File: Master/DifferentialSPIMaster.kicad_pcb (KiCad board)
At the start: 2 copper layers, 52.7 x 36.2 mm, 39 parts, among them J1 Motor Encoder 0, J2 Conn_01x20, J3 Motor Encoder 0, U1 SN65HVD06D, U2 SN65HVD06D, U3 SN65HVD06D, U4 SN65HVD06D, U5 SN65HVD06D, U6 SN65HVD06D

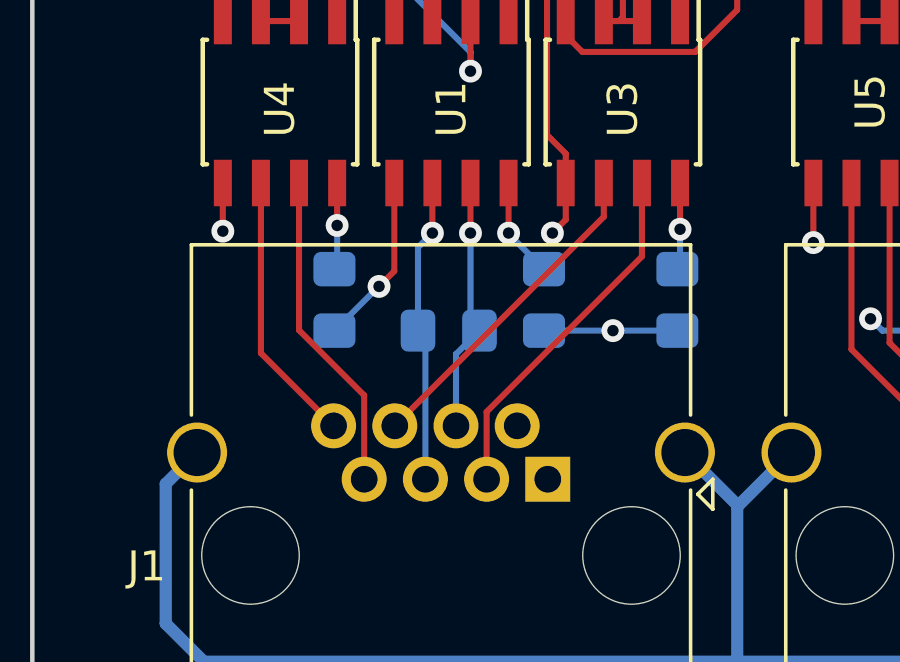
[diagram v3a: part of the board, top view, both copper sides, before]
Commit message: differential tuning on master
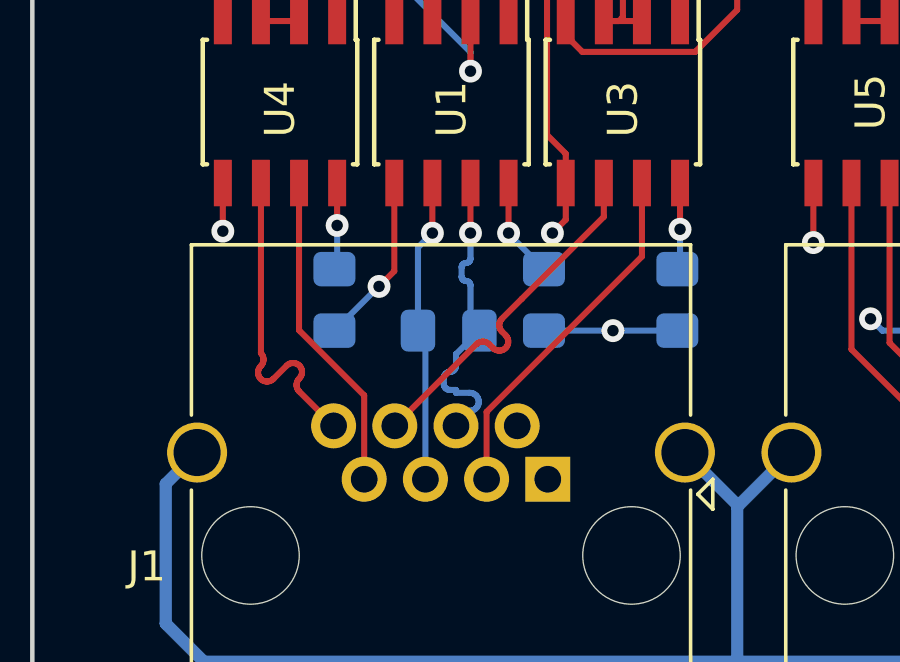
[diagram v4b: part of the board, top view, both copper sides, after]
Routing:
- net /MISO_1_-: track 8.54 -> 10.6 mm
- net /CS_1_+: track 9.10 -> 10.8 mm
- net /CLK_1_+: track 11.0 -> 12.0 mm

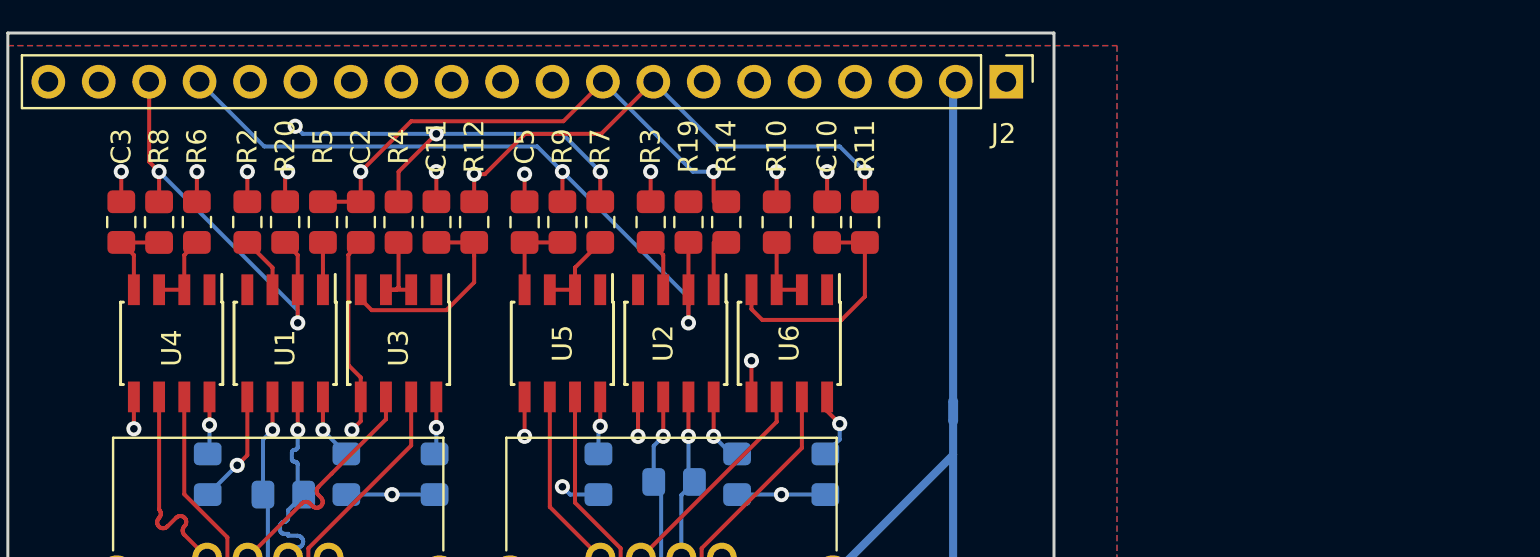
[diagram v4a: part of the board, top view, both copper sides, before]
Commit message: Swap to MAX14783 on Master
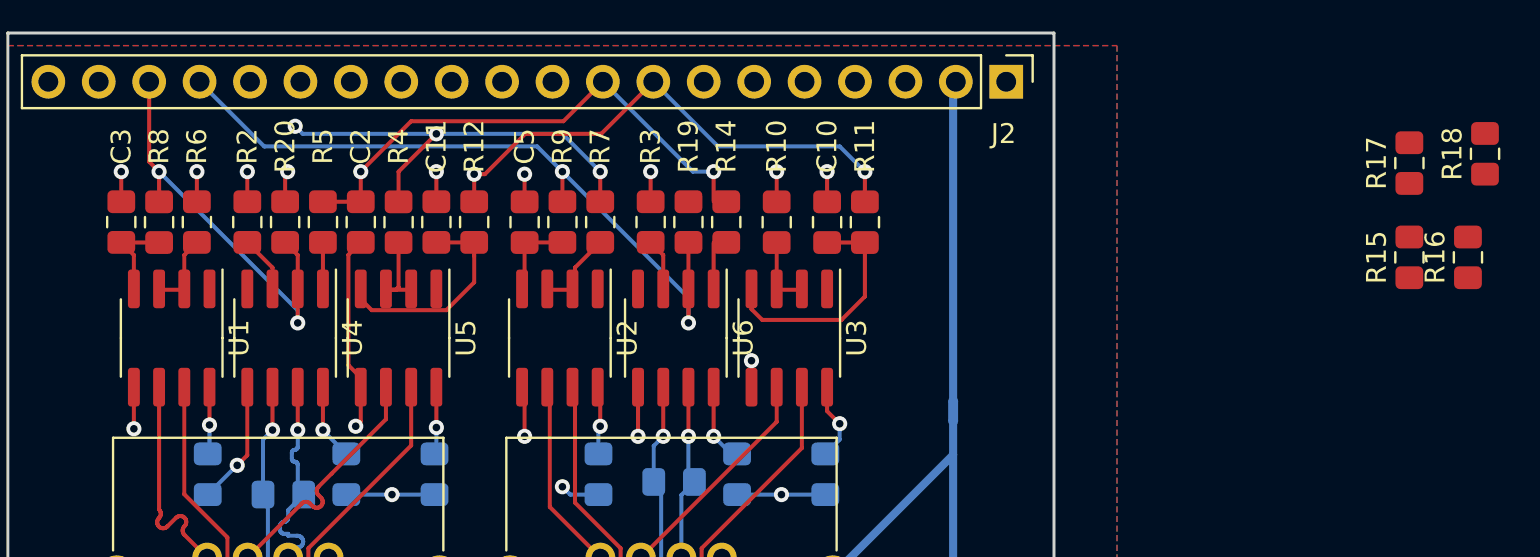
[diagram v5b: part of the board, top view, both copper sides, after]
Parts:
- added R15: 120, Resistor_SMD:R_0805_2012Metric_Pad1.15x1.40mm_HandSolder, F.Cu at (164.5, 98.4)
- added R16: 120, Resistor_SMD:R_0805_2012Metric_Pad1.15x1.40mm_HandSolder, F.Cu at (167.4, 98.4)
- added R17: 120, Resistor_SMD:R_0805_2012Metric_Pad1.15x1.40mm_HandSolder, F.Cu at (164.5, 93.6)
- added R18: 120, Resistor_SMD:R_0805_2012Metric_Pad1.15x1.40mm_HandSolder, F.Cu at (168.3, 93.2)
- U1, U2, U3, U4, U5, U6: value SN65HVD06D -> MAX14783ExS
- moved U3 19.7 mm to (133.2, 102.4)
- moved U5 8.26 mm to (113.5, 102.4)
- moved U2 5.85 mm to (121.7, 102.4)
- moved U1 5.72 mm to (102.1, 102.4)
- moved U4 5.72 mm to (107.8, 102.4)
- moved U6 5.72 mm to (127.5, 102.4)
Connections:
- U1 pad 1: Net-(R5-Pad2) -> Net-(U1-Pad1)
- U1 pad 2: /CS_1 -> Net-(R6-Pad2)
- U1 pad 3: Net-(R2-Pad1) -> Net-(R6-Pad2)
- U1 pad 4: Net-(U1-Pad4) -> Net-(C3-Pad1)
- U1 pad 6: /MISO_1_+ -> /CS_1_+
- U1 pad 7: /MISO_1_- -> /CS_1_-
- U2 pad 1: Net-(R14-Pad2) -> Net-(U2-Pad1)
- U2 pad 2: /CS_2 -> Net-(R7-Pad2)
- U2 pad 3: Net-(R3-Pad1) -> Net-(R7-Pad2)
- U2 pad 4: Net-(U2-Pad4) -> Net-(C5-Pad1)
- U2 pad 6: /MISO_2_+ -> /CS_2_+
- U2 pad 7: /MISO_2_- -> /CS_2_-
- U3 pad 2: Net-(R4-Pad2) -> Net-(R10-Pad2)
- U3 pad 3: Net-(R4-Pad2) -> Net-(R10-Pad2)
- U3 pad 4: Net-(C11-Pad1) -> Net-(C10-Pad1)
- U3 pad 6: /CLK_1_+ -> /CLK_2_+
- U3 pad 7: /CLK_1_- -> /CLK_2_-
- U4 pad 1: Net-(U4-Pad1) -> Net-(R5-Pad2)
- U4 pad 2: Net-(R6-Pad2) -> /CS_1
- U4 pad 3: Net-(R6-Pad2) -> Net-(R2-Pad1)
- U4 pad 4: Net-(C3-Pad1) -> Net-(U4-Pad4)
- U4 pad 6: /CS_1_+ -> /MISO_1_+
- U4 pad 7: /CS_1_- -> /MISO_1_-
- U5 pad 2: Net-(R7-Pad2) -> Net-(R4-Pad2)
- U5 pad 3: Net-(R7-Pad2) -> Net-(R4-Pad2)
- U5 pad 4: Net-(C5-Pad1) -> Net-(C11-Pad1)
- U5 pad 6: /CS_2_+ -> /CLK_1_+
- U5 pad 7: /CS_2_- -> /CLK_1_-
- U6 pad 1: Net-(U6-Pad1) -> Net-(R14-Pad2)
- U6 pad 2: Net-(R10-Pad2) -> /CS_2
- U6 pad 3: Net-(R10-Pad2) -> Net-(R3-Pad1)
- U6 pad 4: Net-(C10-Pad1) -> Net-(U6-Pad4)
- U6 pad 6: /CLK_2_+ -> /MISO_2_+
- U6 pad 7: /CLK_2_- -> /MISO_2_-

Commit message: Update master
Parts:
- removed H1, H2: MountingHole, MountingHole:MountingHole_3.5mm
- C1: value 100nF -> C_Small; moved to F.Cu
- C10, C11, C3: value 2.2pF -> C_Small
- C4, C6, C7, C8, C9, R1: moved to F.Cu
- C5: value 2.2pF -> 100nF
- J1: value Motor Encoder 0 -> RJ45_Shielded
- J2: value Conn_01x20 -> RJ45_Shielded; footprint Connector_PinHeader_2.54mm:PinHeader_1x20_P2.54mm_Vertical -> Connector_RJ:RJ45_Amphenol_RJHSE5380
- J3: value Motor Encoder 0 -> Conn_01x20; footprint Connector_RJ:RJ45_Amphenol_RJHSE5380 -> Connector_PinSocket_2.54mm:PinSocket_1x20_P2.54mm_Vertical
- NT1: value Net-Tie_2 -> NetTie_2; moved to F.Cu
- R10, R2, R7, R8, R9: value 1k -> 120
- R11, R12, R14, R3, R4: value 1k -> R_Small
- R13: value 120 -> 1k; moved to F.Cu
- R15, R17, R18: value 120 -> 1k
- R16: value 120 -> R_Small
- R19, R20: value 10k -> 1k
- moved R16 74.1 mm to (94.9, 83.3), turned to 0 degrees
- moved R17 73.8 mm to (94.9, 118.2), turned to 180 degrees
- moved R18 73.4 mm to (94.9, 94.1), turned to 180 degrees
- moved J2 72.8 mm to (71.4, 89.2), turned to 90 degrees
- moved R15 70.8 mm to (94.9, 85.2), turned to 0 degrees
- moved NT1 67.8 mm to (76.1, 123.9), turned to 0 degrees
- moved J3 51.0 mm to (99.6, 75.0), turned to 0 degrees
- moved C4 50.0 mm to (87.2, 123.9), turned to 0 degrees
- moved R11 49.2 mm to (94.9, 122.0), turned to 180 degrees
- moved R10 48.9 mm to (83.7, 94.3), turned to 90 degrees
- moved C10 46.6 mm to (94.9, 120.1), turned to 0 degrees
- moved C7 46.0 mm to (87.5, 80.7), turned to 0 degrees
- moved U3 45.4 mm to (88.8, 111.8), turned to 180 degrees
- moved C6 44.2 mm to (87.9, 97.9), turned to 0 degrees
- moved R7 42.8 mm to (83.7, 111.8), turned to 90 degrees
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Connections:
- C1 pad 1: +5V -> Net-(C1-Pad1)
- C5 pad 1: Net-(C5-Pad1) -> +5V
- J1 pad 3: /CLK_1_- -> /CLK_2_-
- J1 pad 4: /MISO_1_- -> /MISO_2_-
- J1 pad 5: /MISO_1_+ -> /MISO_2_+
- J1 pad 6: /CLK_1_+ -> /CLK_2_+
- J1 pad 7: /CS_1_- -> /CS_2_-
- J1 pad 8: /CS_1_+ -> /CS_2_+
- J1 pad SH: GND -> GNDA
- J2 pad 1: +5V -> GNDD
- J2 pad 2: GNDD -> +5V
- J2 pad 3: Net-(J2-Pad3) -> /CLK_1_-
- J2 pad 4: Net-(J2-Pad4) -> /MISO_1_-
- J2 pad 5: GNDD -> /MISO_1_+
- J2 pad 6: Net-(J2-Pad6) -> /CLK_1_+
- J2 pad 7: Net-(J2-Pad7) -> /CS_1_-
- J2 pad 8: /SPI_SCK -> /CS_1_+
- J3 pad 1: GNDD -> +5V
- J3 pad 2: +5V -> GNDD
- J3 pad 3: /CLK_2_- -> (no net)
- J3 pad 4: /MISO_2_- -> (no net)
- J3 pad 5: /MISO_2_+ -> GNDD
- J3 pad 6: /CLK_2_+ -> (no net)
- J3 pad 7: /CS_2_- -> (no net)
- J3 pad 8: /CS_2_+ -> /SPI_SCK
- NT1 pad 1: GND -> GNDA
- R1 pad 1: /MISO_1_- -> /CS_2_-
- R1 pad 2: /MISO_1_+ -> /CS_2_+
- R10 pad 1: +5V -> /CLK_1_-
- R10 pad 2: Net-(R10-Pad2) -> /CLK_1_+
- R11 pad 1: Net-(C10-Pad1) -> +5V
- R11 pad 2: /SPI_SCK -> Net-(R11-Pad2)
- R12 pad 1: Net-(C11-Pad1) -> +5V
- R12 pad 2: /SPI_SCK -> Net-(R12-Pad2)
- R13 pad 1: /MISO_2_- -> /CS_2
- R13 pad 2: /MISO_2_+ -> +5V
- R14 pad 1: /MISO -> Net-(R14-Pad1)
- R14 pad 2: Net-(R14-Pad2) -> GNDD
- R15 pad 1: /CS_1_- -> /CS_1
- R15 pad 2: /CS_1_+ -> +5V
- R16 pad 1: /CS_2_- -> Net-(R16-Pad1)
- R16 pad 2: /CS_2_+ -> GNDD
- R17 pad 1: /CLK_2_- -> /SPI_SCK
- R17 pad 2: /CLK_2_+ -> Net-(C10-Pad1)
- R18 pad 1: /CLK_1_- -> /SPI_SCK
- R18 pad 2: /CLK_1_+ -> Net-(C11-Pad1)
- R19 pad 1: +5V -> /MISO
- R19 pad 2: /CS_2 -> Net-(R19-Pad2)
- R2 pad 1: Net-(R2-Pad1) -> /CS_1_-
- R2 pad 2: GNDD -> /CS_1_+
- R20 pad 1: +5V -> /MISO
- R20 pad 2: /CS_1 -> Net-(R20-Pad2)
- R3 pad 1: Net-(R3-Pad1) -> +5V
- R3 pad 2: GNDD -> Net-(R3-Pad2)
- R5 pad 1: /MISO -> /CS_2
- R5 pad 2: Net-(R5-Pad2) -> Net-(C1-Pad1)
- R6 pad 1: +5V -> /CS_1
- R6 pad 2: Net-(R6-Pad2) -> Net-(C3-Pad1)
- R7 pad 1: +5V -> /MISO_2_-
- R7 pad 2: Net-(R7-Pad2) -> /MISO_2_+
- R8 pad 1: Net-(C3-Pad1) -> /CLK_2_-
- R8 pad 2: /CS_1 -> /CLK_2_+
- R9 pad 1: Net-(C5-Pad1) -> /MISO_1_-
- R9 pad 2: /CS_2 -> /MISO_1_+
- U1 pad 1: Net-(U1-Pad1) -> (no net)
- U1 pad 2: Net-(R6-Pad2) -> Net-(R3-Pad2)
- U1 pad 3: Net-(R6-Pad2) -> Net-(R3-Pad2)
- U1 pad 4: Net-(C3-Pad1) -> Net-(C1-Pad1)
- U1 pad 6: /CS_1_+ -> /CS_2_+
- U1 pad 7: /CS_1_- -> /CS_2_-
- U2 pad 1: Net-(U2-Pad1) -> (no net)
- U2 pad 2: Net-(R7-Pad2) -> Net-(R4-Pad2)
- U2 pad 3: Net-(R7-Pad2) -> Net-(R4-Pad2)
- U2 pad 4: Net-(C5-Pad1) -> Net-(C3-Pad1)
- U2 pad 6: /CS_2_+ -> /CS_1_+
- U2 pad 7: /CS_2_- -> /CS_1_-
- U3 pad 1: Net-(U3-Pad1) -> Net-(R19-Pad2)
- U3 pad 2: Net-(R10-Pad2) -> /CS_2
- U3 pad 3: Net-(R10-Pad2) -> Net-(R14-Pad1)
- U3 pad 4: Net-(C10-Pad1) -> (no net)
- U3 pad 6: /CLK_2_+ -> /MISO_2_+
- U3 pad 7: /CLK_2_- -> /MISO_2_-
- U4 pad 1: Net-(R5-Pad2) -> (no net)
- U4 pad 2: /CS_1 -> Net-(R11-Pad2)
- U4 pad 3: Net-(R2-Pad1) -> Net-(R11-Pad2)
- U4 pad 4: Net-(U4-Pad4) -> Net-(C10-Pad1)
- U4 pad 6: /MISO_1_+ -> /CLK_2_+
- U4 pad 7: /MISO_1_- -> /CLK_2_-
- U5 pad 1: Net-(U5-Pad1) -> Net-(R20-Pad2)
- U5 pad 2: Net-(R4-Pad2) -> /CS_1
- U5 pad 3: Net-(R4-Pad2) -> Net-(R16-Pad1)
- U5 pad 4: Net-(C11-Pad1) -> (no net)
- U5 pad 6: /CLK_1_+ -> /MISO_1_+
- U5 pad 7: /CLK_1_- -> /MISO_1_-
- U6 pad 1: Net-(R14-Pad2) -> (no net)
- U6 pad 2: /CS_2 -> Net-(R12-Pad2)
- U6 pad 3: Net-(R3-Pad1) -> Net-(R12-Pad2)
- U6 pad 4: Net-(U6-Pad4) -> Net-(C11-Pad1)
- U6 pad 6: /MISO_2_+ -> /CLK_1_+
- U6 pad 7: /MISO_2_- -> /CLK_1_-
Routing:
- net GND: track 81.2 -> 0.00 mm
- net GNDA: track 0.00 -> 79.4 mm
- net +5V: track 45.7 -> 12.6 mm, vias 12 -> 0
- net /CS_1: track 21.1 -> 50.6 mm, vias 2 -> 1
- net GNDD: track 59.3 -> 39.9 mm, vias 15 -> 18
- net /MISO: track 26.5 -> 39.0 mm, vias 2 -> 1
- net /SPI_SCK: track 26.4 -> 37.8 mm, vias 2 -> 0
- net /CS_2: track 36.0 -> 26.8 mm, vias 2 -> 0
- net Net-(C10-Pad1): track 12.0 -> 4.51 mm
- net /CS_2_+: track 9.15 -> 16.2 mm
- net /CLK_1_-: track 12.0 -> 18.8 mm, vias 0 -> 1
- net /CS_2_-: track 10.8 -> 17.3 mm
- net /CS_1_-: track 10.8 -> 17.2 mm
- net Net-(C11-Pad1): track 10.9 -> 4.51 mm
- net /CLK_2_-: track 12.0 -> 18.1 mm, vias 0 -> 1
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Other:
- board size 52.7 x 36.2 mm -> 40.6 x 54.6 mm
- net class Default removed
